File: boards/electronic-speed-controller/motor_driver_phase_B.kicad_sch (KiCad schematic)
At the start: 18 parts, among them U2 MIC4605-2YM-TR, U3 SISHA14DN-T1-GE3, U4 SISHA14DN-T1-GE3, U5 INA180A3IDBVR

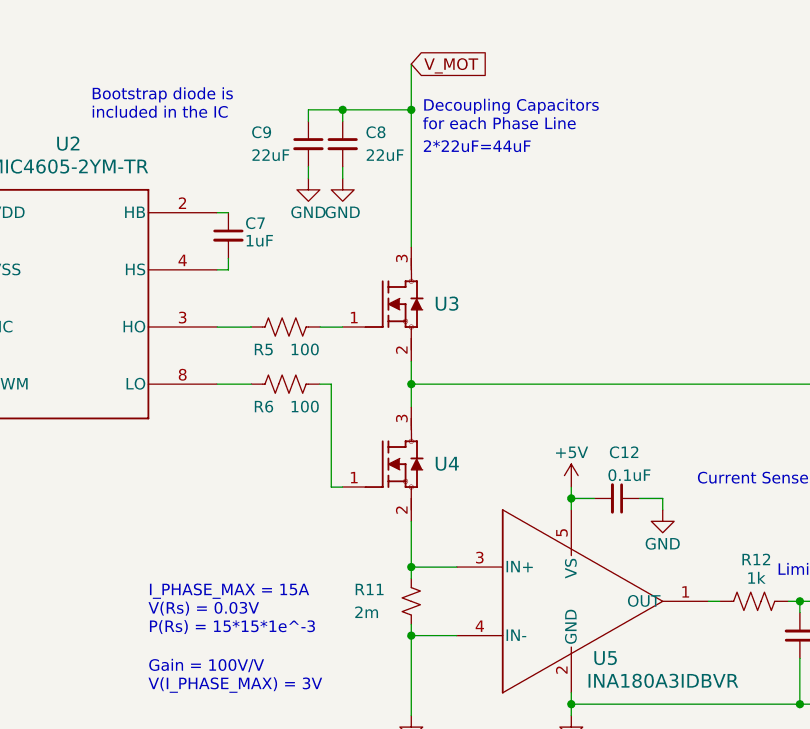
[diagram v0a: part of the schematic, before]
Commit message: updated MOSFETs
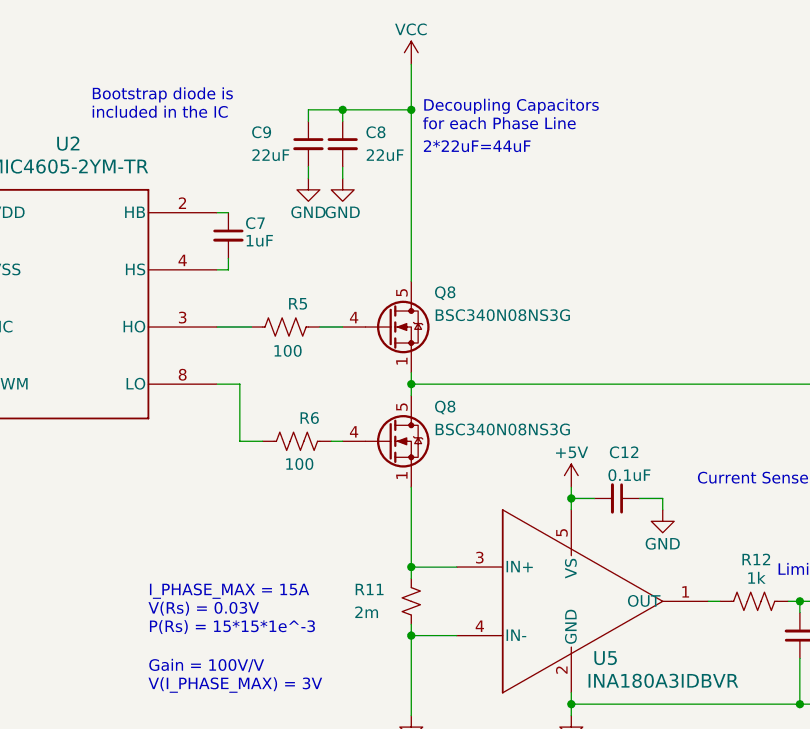
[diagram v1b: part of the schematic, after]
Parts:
- removed U3, U4: SISHA14DN-T1-GE3, MOSFET_3DN-T1-GE3_VIS, symbol N-Channel MOSFET:SISHA14DN-T1-GE3
- added Q8 (x2): BSC340N08NS3G, Package_TO_SOT_SMD:TDSON-8-1, symbol Transistor_FET:BSC340N08NS3G
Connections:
- net V_MOT is gone; now on net VCC: C8.1, C9.1
- net PHASE_B: now also Q8.1 (S), Q8.2 (S), Q8.3 (S), Q8.5 (D)
- net VCC: now also Q8.5 (D)
- net at R5.2: now also Q8.4 (G)
- net at R6.2: now also Q8.4 (G)
- net at R11.1, U5.3 (IN+): now also Q8.1 (S), Q8.2 (S), Q8.3 (S)
